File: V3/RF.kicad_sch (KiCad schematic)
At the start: 5 parts

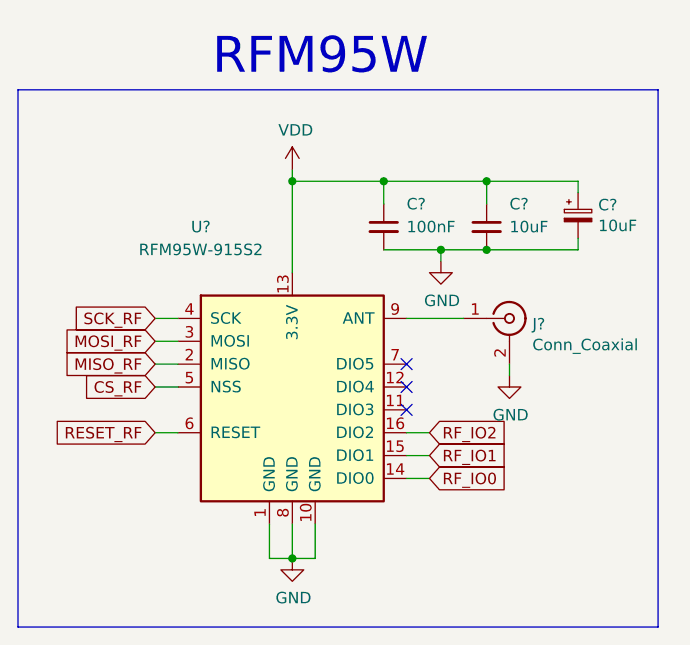
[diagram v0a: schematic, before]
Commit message: Added sims, updated V3 board
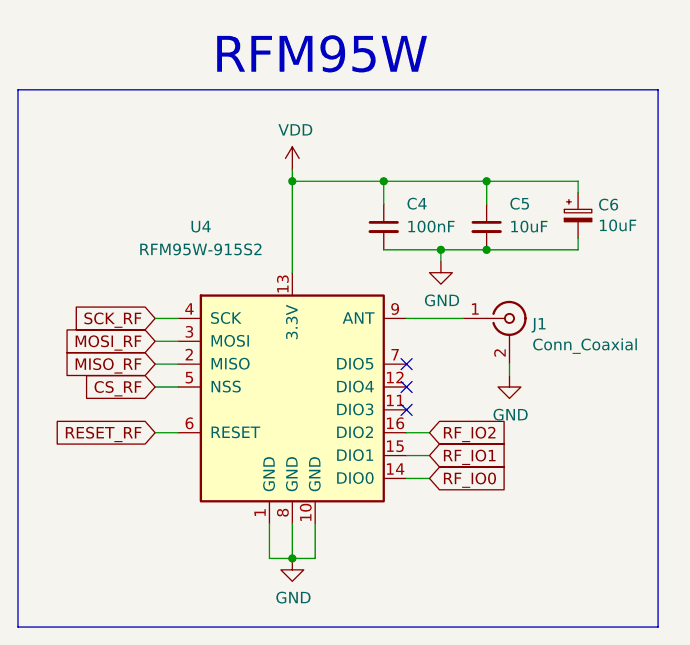
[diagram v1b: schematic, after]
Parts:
- gave numbers to parts that had none: 5
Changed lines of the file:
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@@
   (symbol (lib_id "Device:C_Small") (at 91.44 69.215 0) (unit 1)
     (in_bom yes) (on_board yes)
-    (property "Reference" "C?" (id 0) (at 93.98 66.675 0)
+    (property "Reference" "C5" (id 0) (at 93.98 66.675 0)
       (effects (font (size 1.27 1.27)) (justify left))
     )
@@
   (symbol (lib_id "power:GND") (at 93.98 85.725 0) (unit 1)
     (in_bom yes) (on_board yes)
-    (property "Reference" "#PWR?" (id 0) (at 93.98 92.075 0)
+    (property "Reference" "#PWR0110" (id 0) (at 93.98 92.075 0)
       (effects (font (size 1.27 1.27)) hide)
     )
@@
   (symbol (lib_id "power:VDD") (at 69.85 62.865 0) (unit 1)
     (in_bom yes) (on_board yes)
-    (property "Reference" "#PWR?" (id 0) (at 69.85 66.675 0)
+    (property "Reference" "#PWR0112" (id 0) (at 69.85 66.675 0)
       (effects (font (size 1.27 1.27)) hide)
     )
@@
   (symbol (lib_id "RF_Module:RFM95W-915S2") (at 69.85 86.995 0) (unit 1)
     (in_bom yes) (on_board yes)
-    (property "Reference" "U?" (id 0) (at 59.69 69.215 0))
+    (property "Reference" "U4" (id 0) (at 59.69 69.215 0))
     (property "Value" "RFM95W-915S2" (id 1) (at 59.69 71.755 0))
     (property "Footprint" "RF_Module:HOPERF_RFM9XW_SMD" (id 2) (at -13.97 45.085 0)
@@
   (symbol (lib_id "Device:C_Small") (at 80.01 69.215 0) (unit 1)
     (in_bom yes) (on_board yes)
-    (property "Reference" "C?" (id 0) (at 82.55 66.675 0)
+    (property "Reference" "C4" (id 0) (at 82.55 66.675 0)
       (effects (font (size 1.27 1.27)) (justify left))
     )
@@
   (symbol (lib_id "Device:CP_Small") (at 101.6 67.945 0) (unit 1)
     (in_bom yes) (on_board yes)
-    (property "Reference" "C?" (id 0) (at 103.8352 66.7766 0)
+    (property "Reference" "C6" (id 0) (at 103.8352 66.7766 0)
       (effects (font (size 1.27 1.27)) (justify left))
     )
@@
   (symbol (lib_id "power:GND") (at 69.85 106.045 0) (unit 1)
     (in_bom yes) (on_board yes)
-    (property "Reference" "#PWR?" (id 0) (at 69.85 112.395 0)
+    (property "Reference" "#PWR0113" (id 0) (at 69.85 112.395 0)
       (effects (font (size 1.27 1.27)) hide)
     )
@@
   (symbol (lib_id "power:GND") (at 86.36 73.025 0) (unit 1)
     (in_bom yes) (on_board yes)
-    (property "Reference" "#PWR?" (id 0) (at 86.36 79.375 0)
+    (property "Reference" "#PWR0111" (id 0) (at 86.36 79.375 0)
       (effects (font (size 1.27 1.27)) hide)
     )
@@
   (symbol (lib_id "Connector:Conn_Coaxial") (at 93.98 79.375 0) (unit 1)
     (in_bom yes) (on_board yes)
-    (property "Reference" "J?" (id 0) (at 96.52 80.01 0)
+    (property "Reference" "J1" (id 0) (at 96.52 80.01 0)
       (effects (font (size 1.27 1.27)) (justify left))
     )

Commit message: Added mpu6050 back
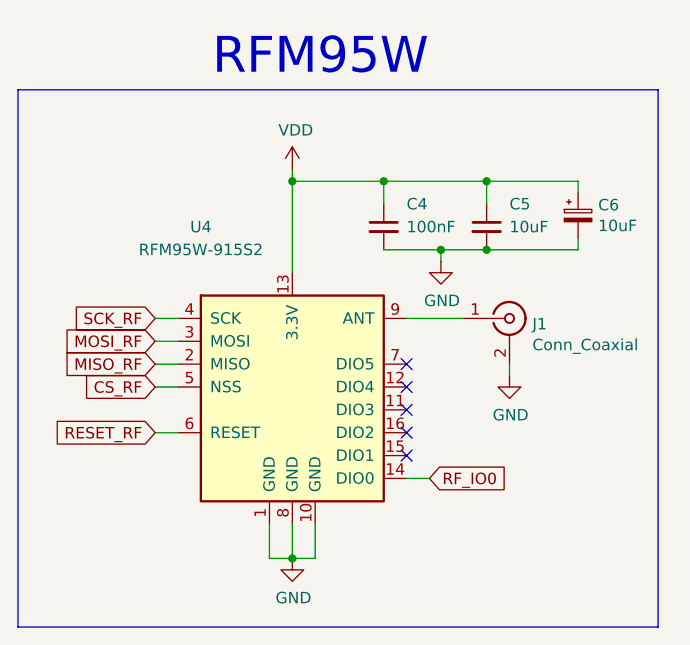
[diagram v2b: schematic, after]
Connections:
- net RF_IO1: no longer names the net of U4.15 (DIO1)
- net RF_IO2: no longer names the net of U4.16 (DIO2)
- no-connect marks 3 -> 5
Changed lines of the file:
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@@
   (no_connect (at 82.55 86.995))
   (no_connect (at 82.55 84.455))
+  (no_connect (at 82.55 92.075))
+  (no_connect (at 82.55 94.615))
   (no_connect (at 82.55 89.535))
   (wire (pts (xy 54.61 84.455) (xy 57.15 84.455))
@@
   )
   (wire (pts (xy 93.98 84.455) (xy 93.98 85.725))
-    (stroke (width 0) (type default) (color 0 0 0 0))
-  )
-  (wire (pts (xy 82.55 92.075) (xy 85.09 92.075))
     (stroke (width 0) (type default) (color 0 0 0 0))
   )
@@
     (stroke (width 0) (type default) (color 0 0 0 0))
   )
-  (wire (pts (xy 82.55 94.615) (xy 85.09 94.615))
-    (stroke (width 0) (type default) (color 0 0 0 0))
-  )
   (wire (pts (xy 80.01 64.135) (xy 91.44 64.135))
     (stroke (width 0) (type default) (color 0 0 0 0))
@@
     (property "Intersheet References" "${INTERSHEET_REFS}" (id 0) (at -271.78 -55.245 0)
       (effects (font (size 1.27 1.27)) hide)
-    )
-  )
-  (global_label "RF_IO2" (shape input) (at 85.09 92.075 0) (fields_autoplaced)
-    (effects (font (size 1.27 1.27)) (justify left))
-    (property "Intersheet References" "${INTERSHEET_REFS}" (id 0) (at -271.78 -55.245 0)
-      (effects (font (size 1.27 1.27)) hide)
-    )
-  )
-  (global_label "RF_IO1" (shape input) (at 85.09 94.615 0) (fields_autoplaced)
-    (effects (font (size 1.27 1.27)) (justify left))
-    (property "Intersheet References" "${INTERSHEET_REFS}" (id 0) (at -271.78 -55.245 0)
-      (effects (font (size 1.27 1.27)) hide)

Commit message: New parts placed and routed
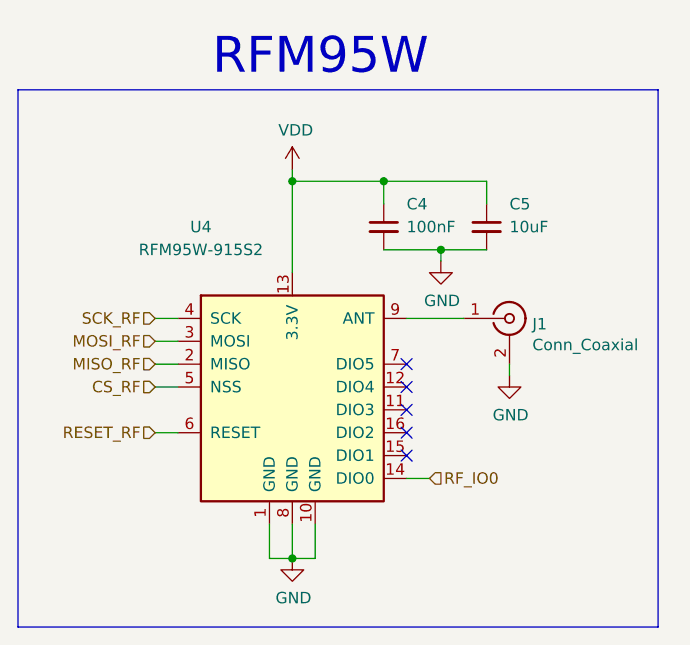
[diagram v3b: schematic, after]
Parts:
- removed C6: 10uF, Capacitor_Tantalum_SMD:CP_EIA-3216-18_Kemet-A, symbol Device:CP_Small
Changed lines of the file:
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@@
 (kicad_sch (version 20211123) (generator eeschema)
   (paper "A4")
-  (junction (at 91.44 64.135) (diameter 0) (color 0 0 0 0)
-  )
   (junction (at 69.85 64.135) (diameter 0) (color 0 0 0 0)
   )
@@
   )
   (junction (at 69.85 106.045) (diameter 0) (color 0 0 0 0)
-  )
-  (junction (at 91.44 71.755) (diameter 0) (color 0 0 0 0)
   )
   (junction (at 80.01 64.135) (diameter 0) (color 0 0 0 0)
@@
     (stroke (width 0) (type default) (color 0 0 0 0))
   )
-  (wire (pts (xy 101.6 64.135) (xy 101.6 65.405))
-    (stroke (width 0) (type default) (color 0 0 0 0))
-  )
   (wire (pts (xy 82.55 97.155) (xy 85.09 97.155))
     (stroke (width 0) (type default) (color 0 0 0 0))
@@
     (stroke (width 0) (type default) (color 0 0 0 0))
   )
-  (wire (pts (xy 101.6 70.485) (xy 101.6 71.755))
-    (stroke (width 0) (type default) (color 0 0 0 0))
-  )
   (wire (pts (xy 69.85 102.235) (xy 69.85 106.045))
     (stroke (width 0) (type default) (color 0 0 0 0))
@@
   )
   (polyline (pts (xy 110.49 53.975) (xy 39.37 53.975))
-    (stroke (width 0) (type default) (color 0 0 0 0))
-  )
-  (wire (pts (xy 91.44 64.135) (xy 101.6 64.135))
-    (stroke (width 0) (type default) (color 0 0 0 0))
-  )
-  (wire (pts (xy 101.6 71.755) (xy 91.44 71.755))
     (stroke (width 0) (type default) (color 0 0 0 0))
   )
@@
     (effects (font (size 3.9878 3.9878)) (justify left bottom))
   )
-  (global_label "MOSI_RF" (shape input) (at 54.61 81.915 180) (fields_autoplaced)
-    (effects (font (size 1.27 1.27)) (justify right))
-    (property "Intersheet References" "${INTERSHEET_REFS}" (id 0) (at -271.78 -55.245 0)
-      (effects (font (size 1.27 1.27)) hide)
-    )
-  )
-  (global_label "MISO_RF" (shape input) (at 54.61 84.455 180) (fields_autoplaced)
-    (effects (font (size 1.27 1.27)) (justify right))
-    (property "Intersheet References" "${INTERSHEET_REFS}" (id 0) (at -271.78 -55.245 0)
-      (effects (font (size 1.27 1.27)) hide)
-    )
-  )
-  (global_label "RESET_RF" (shape input) (at 54.61 92.075 180) (fields_autoplaced)
-    (effects (font (size 1.27 1.27)) (justify right))
-    (property "Intersheet References" "${INTERSHEET_REFS}" (id 0) (at -271.78 -55.245 0)
-      (effects (font (size 1.27 1.27)) hide)
-    )
-  )
-  (global_label "SCK_RF" (shape input) (at 54.61 79.375 180) (fields_autoplaced)
-    (effects (font (size 1.27 1.27)) (justify right))
-    (property "Intersheet References" "${INTERSHEET_REFS}" (id 0) (at -271.78 -55.245 0)
-      (effects (font (size 1.27 1.27)) hide)
-    )
-  )
-  (global_label "CS_RF" (shape input) (at 54.61 86.995 180) (fields_autoplaced)
-    (effects (font (size 1.27 1.27)) (justify right))
-    (property "Intersheet References" "${INTERSHEET_REFS}" (id 0) (at -271.78 -55.245 0)
-      (effects (font (size 1.27 1.27)) hide)
-    )
-  )
-  (global_label "RF_IO0" (shape input) (at 85.09 97.155 0) (fields_autoplaced)
+  (hierarchical_label "RESET_RF" (shape input) (at 54.61 92.075 180)
+    (effects (font (size 1.27 1.27)) (justify right))
+  )
+  (hierarchical_label "CS_RF" (shape input) (at 54.61 86.995 180)
+    (effects (font (size 1.27 1.27)) (justify right))
+  )
+  (hierarchical_label "RF_IO0" (shape input) (at 85.09 97.155 0)
     (effects (font (size 1.27 1.27)) (justify left))
-    (property "Intersheet References" "${INTERSHEET_REFS}" (id 0) (at -271.78 -55.245 0)
-      (effects (font (size 1.27 1.27)) hide)
-    )
+  )
+  (hierarchical_label "MISO_RF" (shape input) (at 54.61 84.455 180)
+    (effects (font (size 1.27 1.27)) (justify right))
+  )
+  (hierarchical_label "SCK_RF" (shape input) (at 54.61 79.375 180)
+    (effects (font (size 1.27 1.27)) (justify right))
+  )
+  (hierarchical_label "MOSI_RF" (shape input) (at 54.61 81.915 180)
+    (effects (font (size 1.27 1.27)) (justify right))
   )
   (symbol (lib_id "Device:C_Small") (at 91.44 69.215 0) (unit 1)
@@
       (effects (font (size 1.27 1.27)) hide)
     )
-    (pin "1")
-    (pin "2")
-  )
-  (symbol (lib_id "Device:CP_Small") (at 101.6 67.945 0) (unit 1)
-    (in_bom yes) (on_board yes)
-    (property "Reference" "C6" (id 0) (at 103.8352 66.7766 0)
-      (effects (font (size 1.27 1.27)) (justify left))
-    )
-    (property "Value" "10uF" (id 1) (at 103.8352 69.088 0)
-      (effects (font (size 1.27 1.27)) (justify left))
-    )
-    (property "Footprint" "Capacitor_Tantalum_SMD:CP_EIA-3216-18_Kemet-A" (id 2) (at 101.6 67.945 0)
-      (effects (font (size 1.27 1.27)) hide)
-    )
-    (property "Datasheet" "~" (id 3) (at 101.6 67.945 0)
-      (effects (font (size 1.27 1.27)) hide)
-    )
